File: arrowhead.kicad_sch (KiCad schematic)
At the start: 145 parts, among them J1 USB_C_Receptacle_USB2.0_14P, J2 USB_C_Receptacle_USB2.0_14P, J3 USB3_A, J4 USB3_A, U1 CH334R, Y1 Crystal_GND23

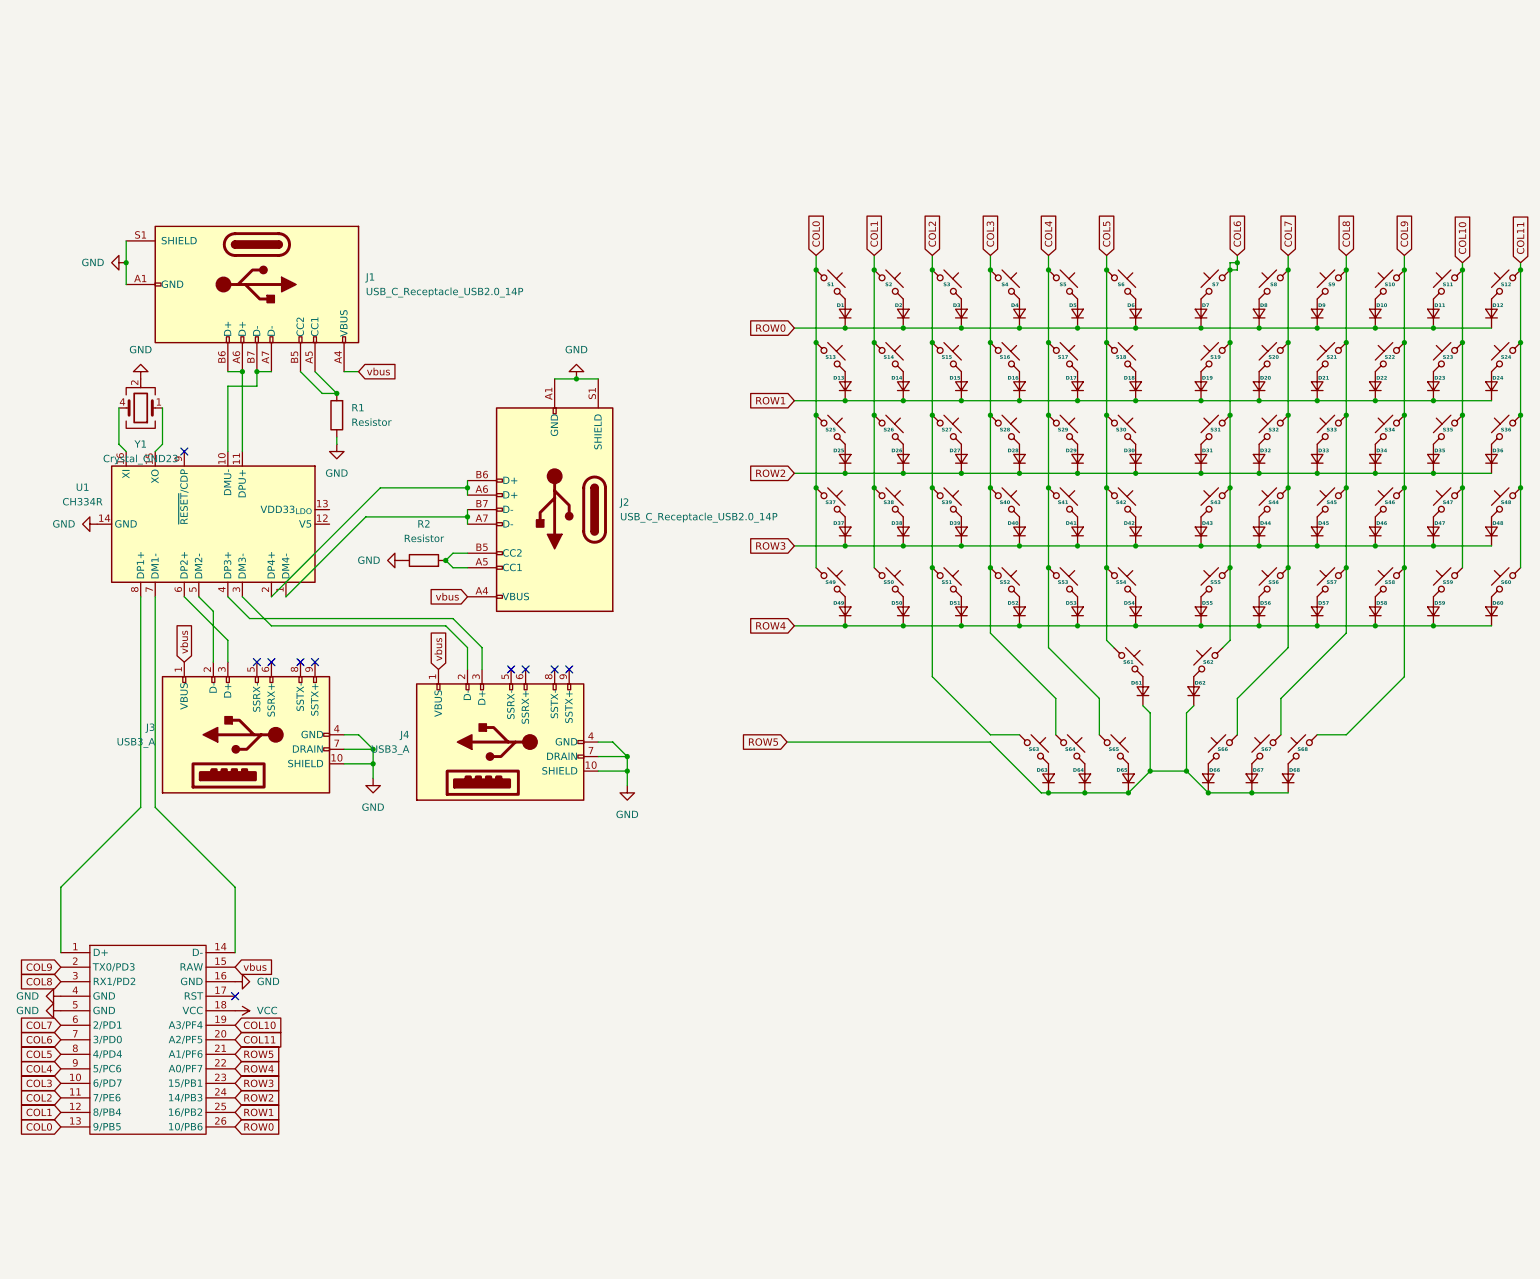
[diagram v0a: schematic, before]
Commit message: realised the ch334 models aren't available from dk, so I had to redesign
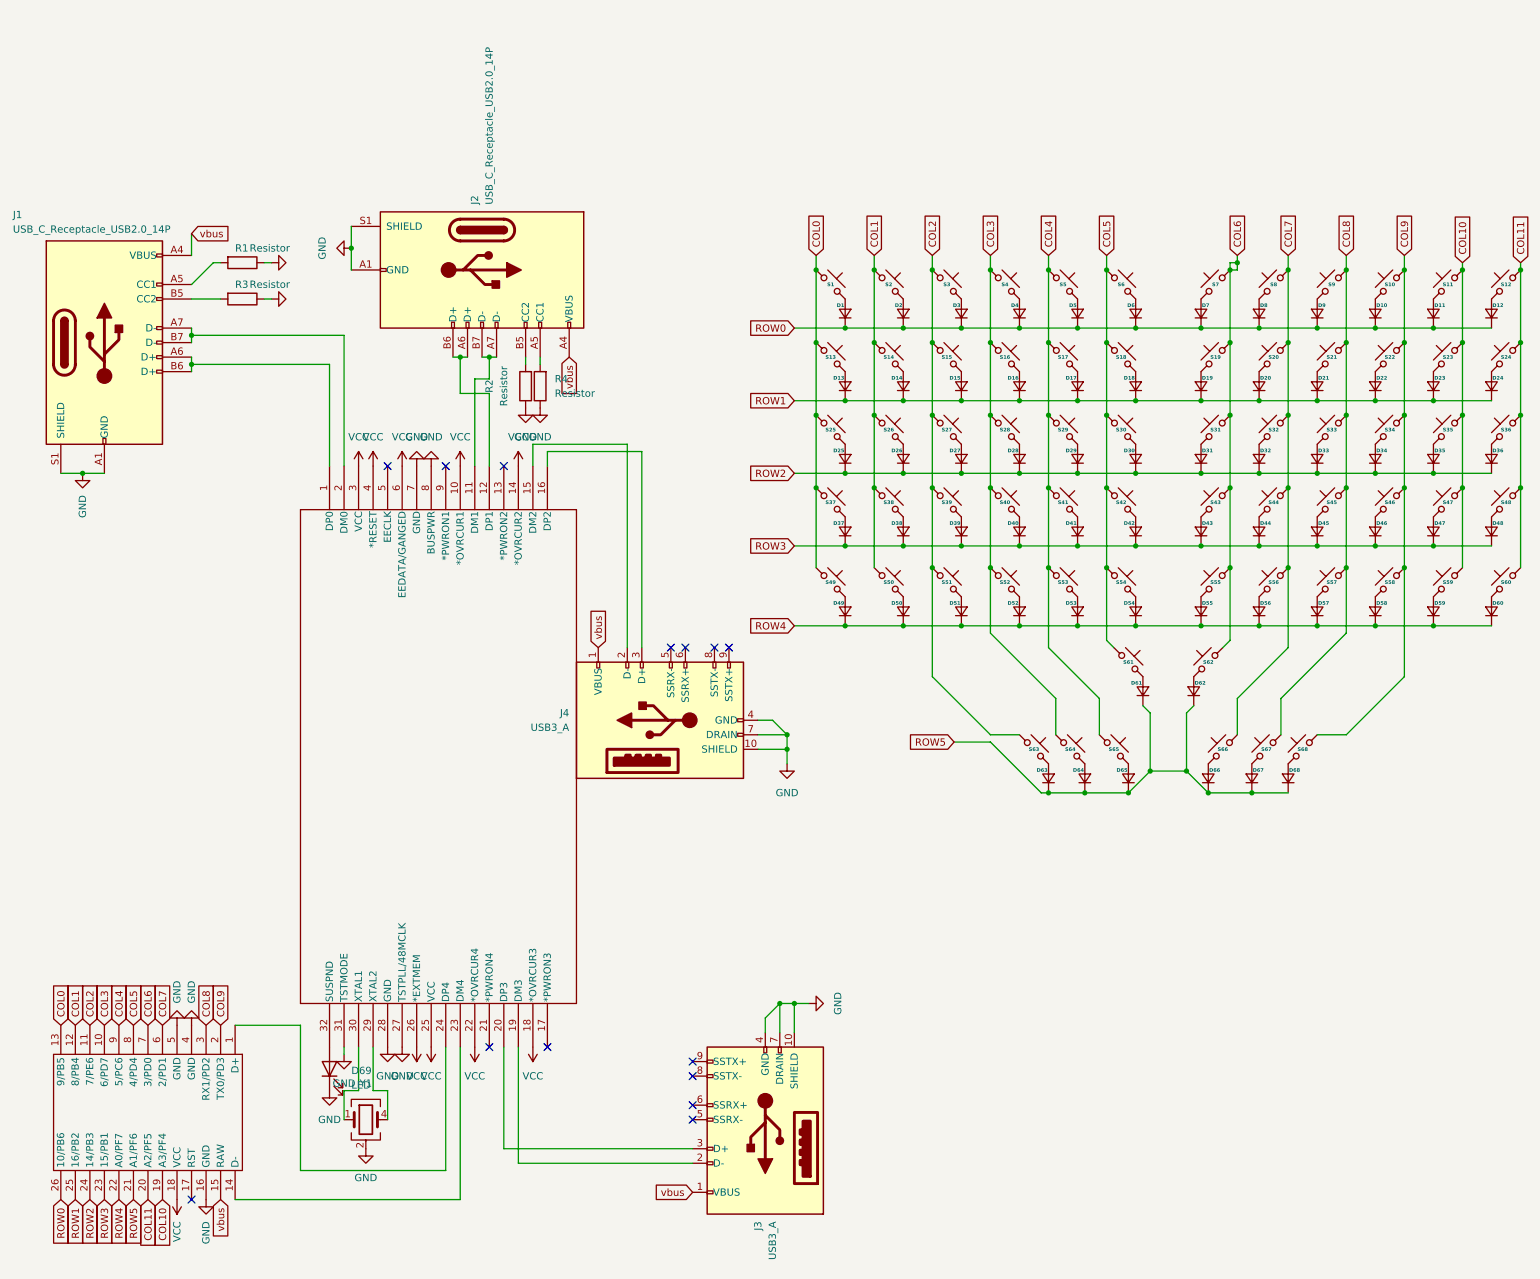
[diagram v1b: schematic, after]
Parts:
- removed U1: CH334R, Package_SO:QSOP-16_3.9x4.9mm_P0.635mm, symbol Interface_USB:CH334R
- added D69: LED, LED_SMD:LED_0201_0603Metric, symbol Device:LED
- added R3, R4: Resistor, ScottoKeebs_Components:Resistor_0402, symbol scotto:Placeholder_Resistor
- added U1: TUSB2046BVF, footprints:VF32, symbol tusb:TUSB2046BVF
- Y1: footprint Crystal:Crystal_SMD_2520-4Pin_2.5x2.0mm -> Crystal:Crystal_SMD_7050-2Pin_7.0x5.0mm
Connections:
- net GND: now also D69.1 (K), R3.1, R4.1, U1.27 (TSTPLL/48MCLK), U1.28 (GND), U1.31 (TSTMODE), U1.7 (GND), U1.8 (BUSPWR)
- net VCC: now also U1.10 (*OVRCUR1), U1.14 (*OVRCUR2), U1.18 (*OVRCUR3), U1.22 (*OVRCUR4), U1.25 (VCC), U1.26 (*EXTMEM), U1.3 (VCC), U1.4 (*RESET), U1.6 (EEDATA/GANGED)
- net at J2.B5 (CC2), R2.2: no longer J2.A5 (CC1)
- net at J4.2 (D-): now also U1.15 (DM2)
- net at J4.3 (D+): now also U1.16 (DP2)
- net at J1.A5 (CC1), R1.2: no longer J1.B5 (CC2)
- net at J1.A6 (D+), J1.B6 (D+): now also U1.1 (DP0)
- net at J1.A7 (D-), J1.B7 (D-): now also U1.2 (DM0)
- net at Y1.1: now also U1.30 (XTAL1)
- net at Y1.4: now also U1.29 (XTAL2)
- net at J2.A6 (D+), J2.B6 (D+): now also U1.12 (DP1)
- net at J2.A7 (D-), J2.B7 (D-): now also U1.11 (DM1)
- net at J3.2 (D-): now also U1.19 (DM3)
- net at J3.3 (D+): now also U1.20 (DP3)
- net at U2.1 (D+): now also U1.24 (DP4)
- net at U2.14 (D-): now also U1.23 (DM4)
- new net: J1.B5 (CC2), R3.2
- new net: D69.2 (A), U1.32 (SUSPND)
- new net: J2.A5 (CC1), R4.2
- no-connect marks 10 -> 14
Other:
- moved on the sheet: J1, J2, J3, J4, R1, R2, Y1

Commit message: production run 1
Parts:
- added C1, C2: C_US, Capacitor_SMD:C_0603_1608Metric_Pad1.08x0.95mm_HandSolder, symbol Device:C_US
- D1, D10, D11, D12, D13, D14, D15, D16, D17, D18, D19, D2, D20, D21, D22, D23, D24, D25, D26, D27, D28, D29, D3, D30, D31, D32, D33, D34, D35, D36, D37, D38, D39, D4, D40, D41, D42, D43, D44, D45, D46, D47, D48, D49, D5, D50, D51, D52, D53, D54, D55, D56, D57, D58, D59, D6, D60, D61, D62, D63, D64, D65, D66, D67, D68, D7, D8, D9, S1, S10, S11, S12, S13, S14, S15, S16, S17, S18, S19, S2, S20, S21, S22, S23, S24, S25, S26, S27, S28, S29, S3, S30, S31, S32, S33, S34, S35, S36, S37, S38, S39, S4, S40, S41, S42, S43, S44, S45, S46, S47, S48, S49, S5, S50, S51, S52, S53, S54, S55, S56, S57, S58, S59, S6, S60, S61, S62, S63, S64, S65, S66, S67, S68, S7, S8, S9, U2: value ~ -> (none)
- D69: footprint LED_SMD:LED_0201_0603Metric -> LED_SMD:LED_0603_1608Metric_Pad1.05x0.95mm_HandSolder
- Y1: footprint Crystal:Crystal_SMD_7050-2Pin_7.0x5.0mm -> Crystal:Crystal_SMD_7050-4Pin_7.0x5.0mm
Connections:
- net GND: now also C1.2, C2.2
- net at Y1.1: now also U1.29 (XTAL2), C1.1; no longer U1.30 (XTAL1)
- net at Y1.4: now also U1.30 (XTAL1), C2.1; no longer U1.29 (XTAL2)
- net at J2.A7 (D-), J2.B7 (D-): now also U1.19 (DM3); no longer U1.11 (DM1)
- net at J2.A6 (D+), J2.B6 (D+): now also U1.20 (DP3); no longer U1.12 (DP1)
- net at J3.2 (D-): now also U1.11 (DM1); no longer U1.19 (DM3)
- net at J3.3 (D+): now also U1.12 (DP1); no longer U1.20 (DP3)
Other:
- moved on the sheet: J2, J3, R2, R4, Y1

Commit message: actual first production run
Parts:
- D69: footprint LED_SMD:LED_0603_1608Metric_Pad1.05x0.95mm_HandSolder -> LED_SMD:LED_0805_2012Metric
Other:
- moved on the sheet: D69
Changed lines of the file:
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@@
 	(symbol
 		(lib_id "Device:LED")
-		(at 72.39 163.83 90)
+		(at 72.39 163.83 270)
+		(mirror x)
 		(unit 1)
 		(body_style 1)
@@
 		(in_pos_files yes)
 		(dnp no)
-		(fields_autoplaced yes)
 		(property "Reference" "D69"
-			(at 76.2 164.1474 90)
+			(at 68.58 164.1474 90)
 			(show_name no)
 			(do_not_autoplace no)
@@
 		)
 		(property "Value" "LED"
-			(at 76.2 166.6874 90)
+			(at 68.58 166.6874 90)
 			(show_name no)
 			(do_not_autoplace no)
@@
 			)
 		)
-		(property "Footprint" "LED_SMD:LED_0603_1608Metric_Pad1.05x0.95mm_HandSolder"
+		(property "Footprint" "LED_SMD:LED_0805_2012Metric"
 			(at 72.39 163.83 0)
 			(hide yes)
